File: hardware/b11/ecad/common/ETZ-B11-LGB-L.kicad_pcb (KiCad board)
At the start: 2 copper layers, 29 x 88.8 mm, 0 parts

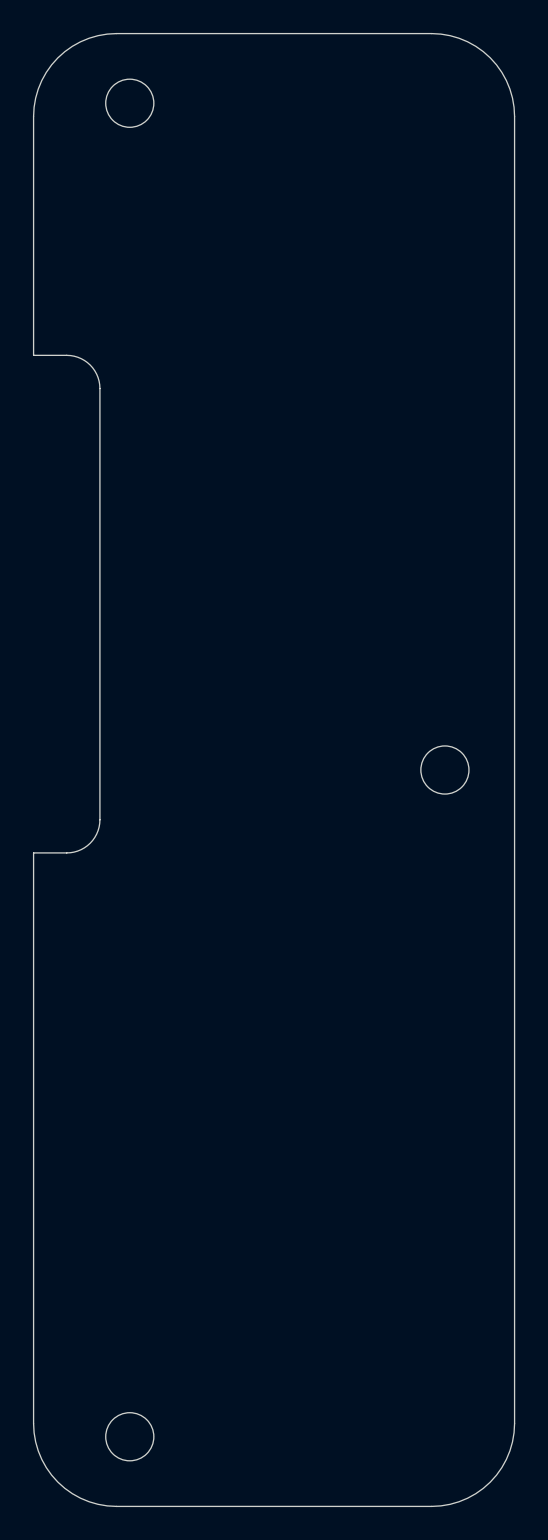
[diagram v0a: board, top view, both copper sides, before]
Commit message: feat: add logic board connector placement
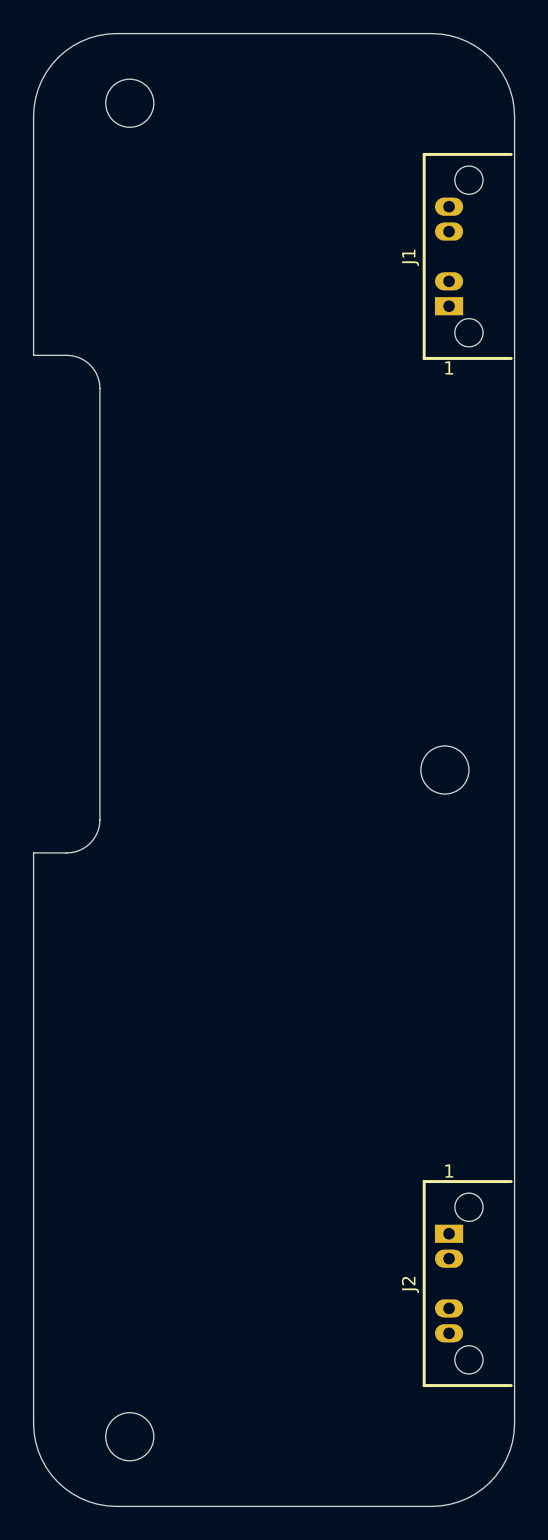
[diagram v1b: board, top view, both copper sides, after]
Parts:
- added J1: CN-HY04C-01D-MALE, CN-HY04C-01D-MALE, F.Cu at (163.0, 74.0)
- added J2: CN-HY04C-01D-FEMALE, CN-HY04C-01D-FEMALE, F.Cu at (163.0, 136.0)

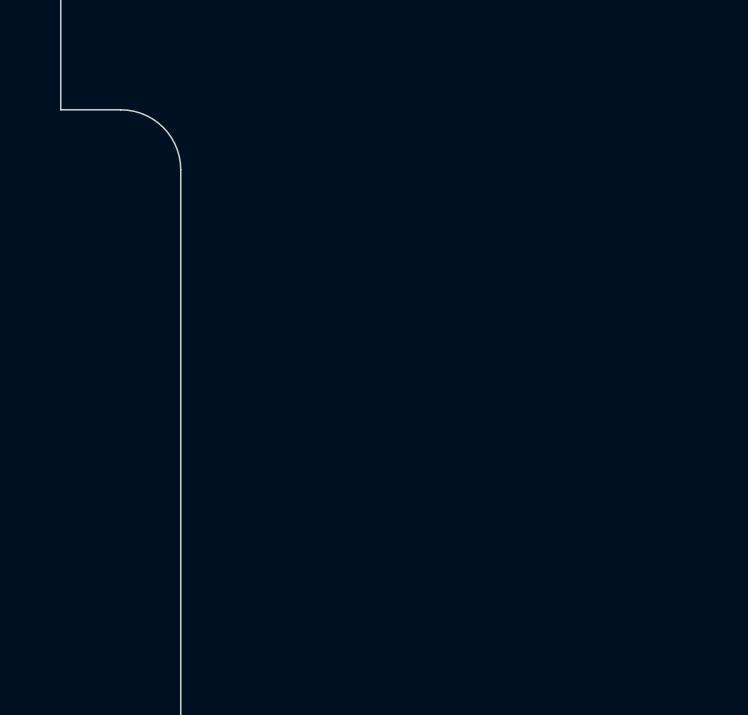
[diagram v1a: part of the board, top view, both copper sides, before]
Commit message: feat: add carrier logic FPC interconnect
Signed-off-by: Nikola Secerovski <secersh@gmail.com>
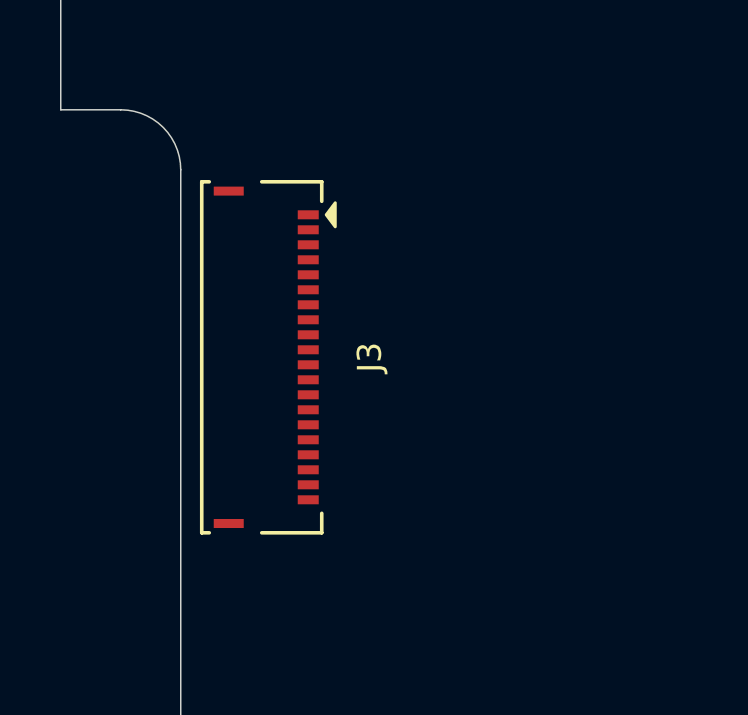
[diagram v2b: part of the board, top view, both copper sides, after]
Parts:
- added J3: 503480-2000, 503480-2000, F.Cu at (139.6, 88.2)
